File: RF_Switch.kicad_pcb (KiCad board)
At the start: 2 copper layers, 38.1 x 38.1 mm, 5 parts, among them J1 Conn_Coaxial, J2 Conn_01x04, J3 Conn_Coaxial, J4 Conn_Coaxial, U1 HSWA2-30DR+

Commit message: Finished REV A
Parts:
- added C1: 100pF, Capacitor_SMD:C_0603_1608Metric, F.Cu at (164.0, 71.1)
- added C2: 0.1uF, Capacitor_SMD:C_0603_1608Metric, F.Cu at (164.0, 69.5)
- added J5: Conn_01x04, lib_fp:Header 4 Keyed RT Angle, F.Cu at (173.8, 80.1)
- added R1: 4.7k, Resistor_SMD:R_0603_1608Metric, F.Cu at (167.5, 69.4)
- added R2: 4.7k, Resistor_SMD:R_0603_1608Metric, F.Cu at (167.5, 70.9)
- J1, J4: footprint Connector_Coaxial:SMA_Amphenol_132289_EdgeMount -> lib_fp:SMA_Taoglas_Limited_Narrow_EdgeMount
- J3: footprint Connector_Coaxial:SMA_Amphenol_132289_EdgeMount -> lib_fp:SMA_Plug_Linx_Technologies_EdgeMount_CONSMA013.062
- moved J4 27.1 mm to (170.0, 62.3), turned to 90 degrees
- moved J1 20.9 mm to (160.0, 62.3), turned to 90 degrees
- moved J2 16.2 mm to (156.2, 80.0), turned to 0 degrees
- moved J3 15.5 mm to (165.0, 85.0)
- moved U1 9.93 mm to (165.0, 75.0)
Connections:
- U1 pad 15: (no net) -> GND
- U1 pad 16: Net-(J2-Pad4) -> Net-(R2-Pad2)
- U1 pad 17: Net-(J2-Pad3) -> Net-(R1-Pad2)
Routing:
- net GND: track 0.00 -> 44.0 mm, vias 0 -> 4
- net Net-(C1-Pad1): track 12.2 -> 28.1 mm, vias 0 -> 1
- net Net-(J2-Pad3): track 12.4 -> 26.5 mm, vias 0 -> 1
- net Net-(J2-Pad4): track 13.3 -> 24.9 mm, vias 0 -> 1
- net Net-(J3-Pad1): track 14.1 -> 8.16 mm
- net Net-(R1-Pad2): track 0.00 -> 4.29 mm
- net Net-(R2-Pad2): track 0.00 -> 2.56 mm
- net Net-(J1-Pad1): track 14.1 -> 15.3 mm
- net Net-(J4-Pad1): track 14.1 -> 15.3 mm
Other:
- board size 38.1 x 38.1 mm -> 20 x 28 mm
- board text added: "3V"
- board text added: "CTL1"
- board text added: "CTL2"
- board text added: "GND"
- board text added: "RF1"
- board text added: "RF2"
- board text added: "RFCOM"

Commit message: Added two vias by the RFCOM port to link top and bottom copper close to this connector
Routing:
- net GND: vias 4 -> 6

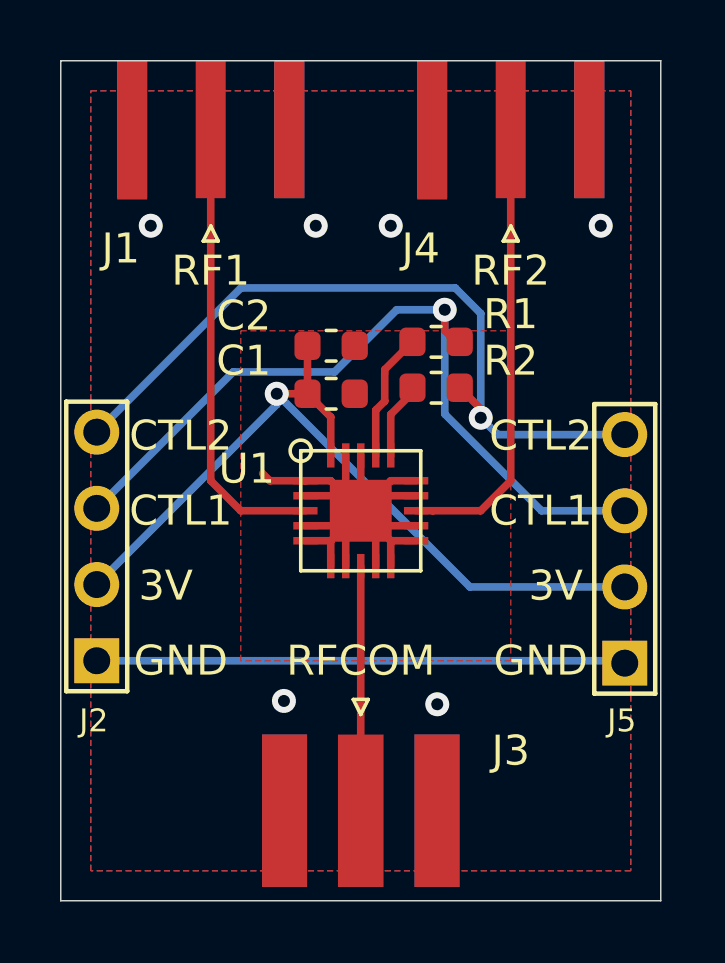
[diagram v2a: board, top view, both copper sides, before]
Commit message: Added lots of vias to tie top and bottom together better
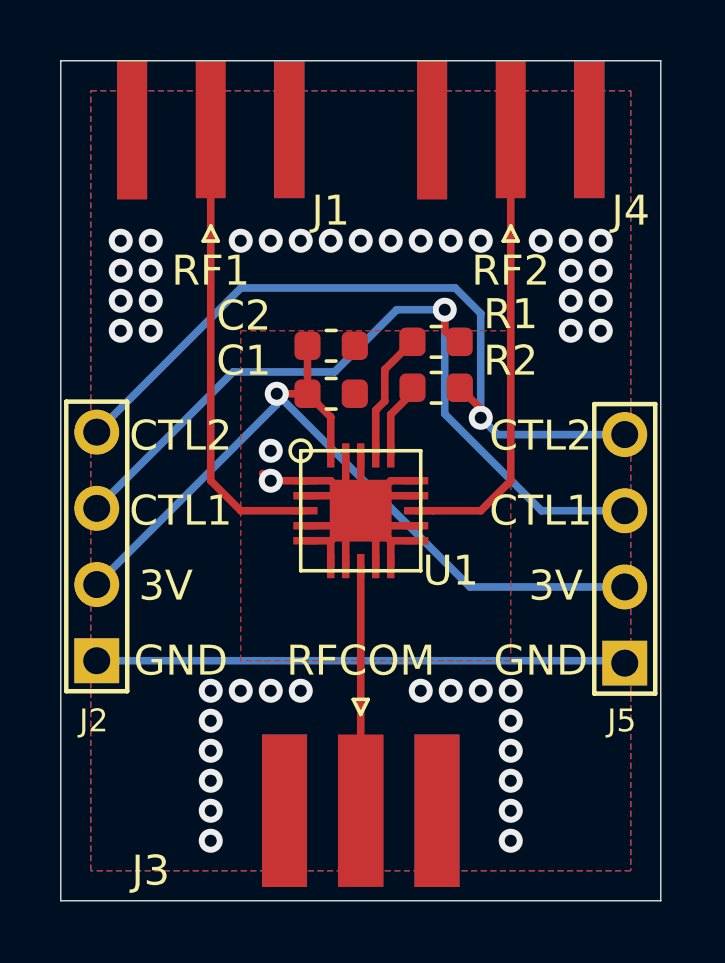
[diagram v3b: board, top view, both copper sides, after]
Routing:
- net GND: vias 6 -> 46
